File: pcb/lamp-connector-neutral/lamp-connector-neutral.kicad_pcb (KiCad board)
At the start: 2 copper layers, 17.8 x 29 mm, 2 parts

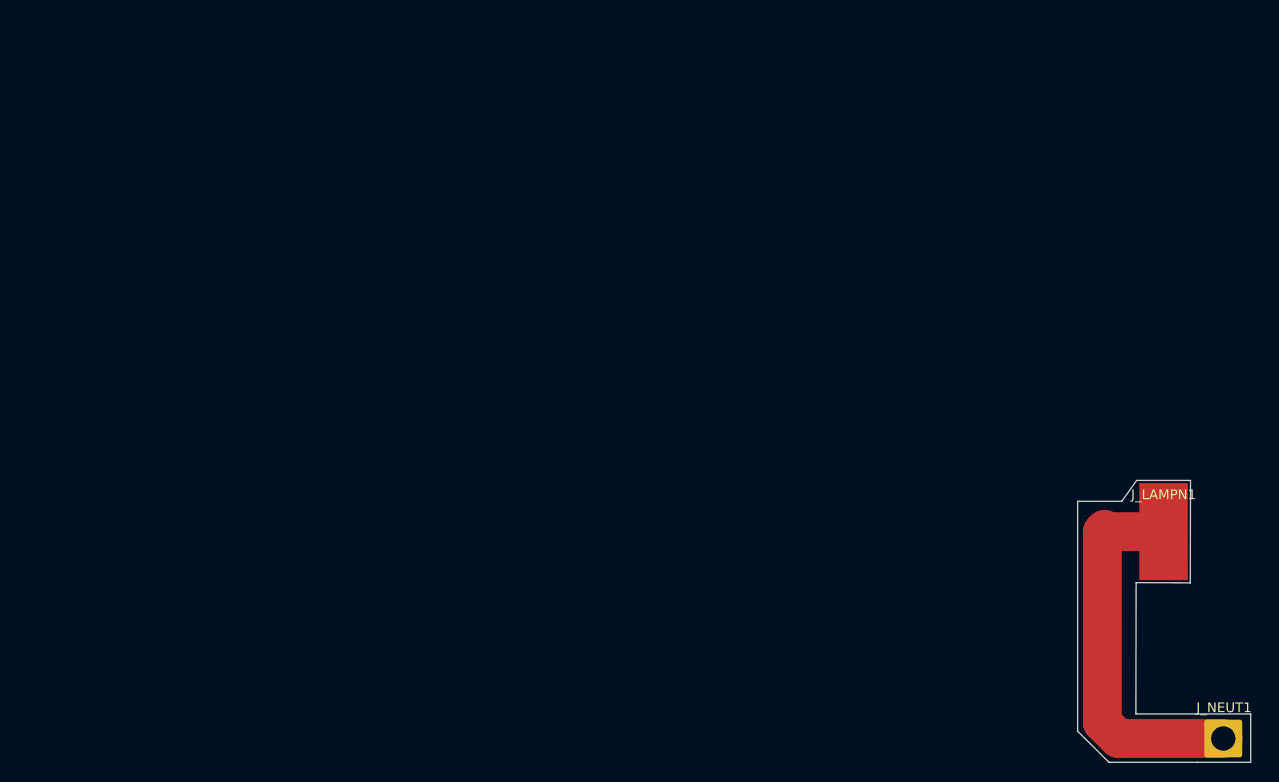
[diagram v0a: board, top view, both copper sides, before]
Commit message: Lamp Connectors
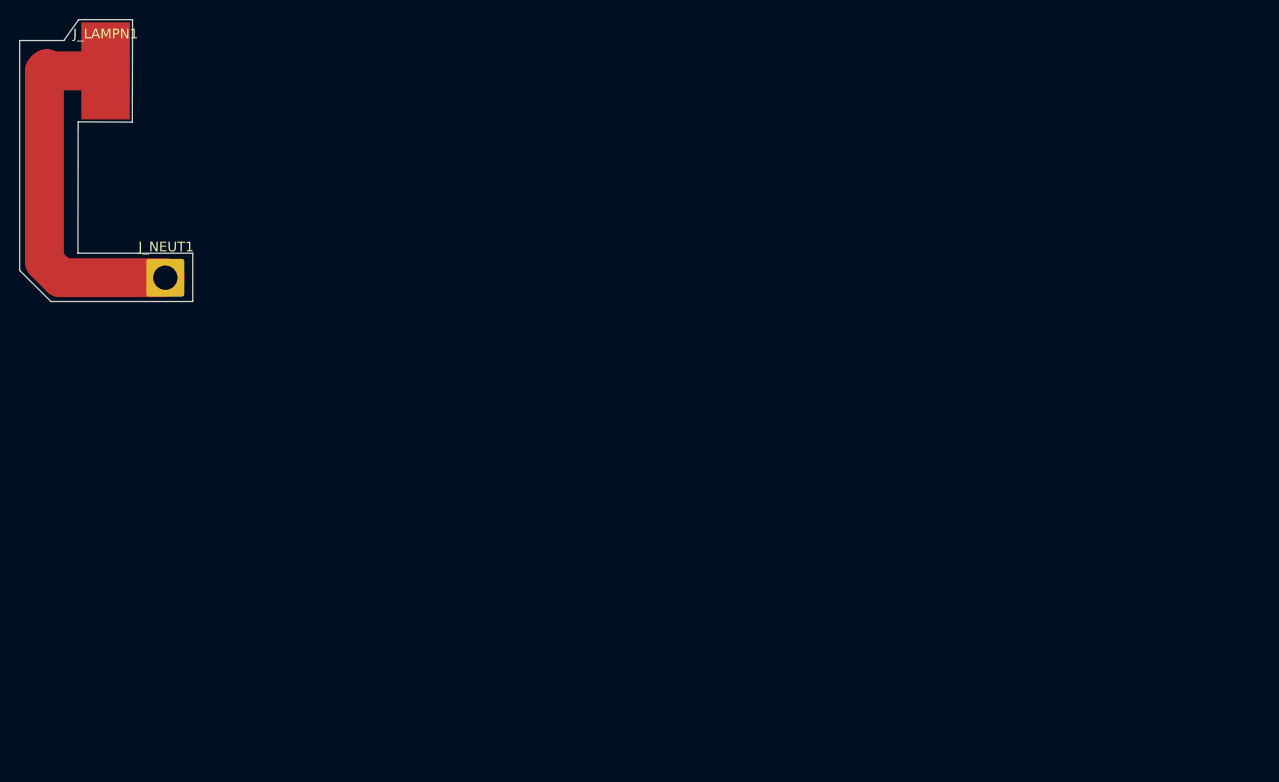
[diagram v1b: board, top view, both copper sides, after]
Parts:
- moved J_LAMPN1 118.8 mm to (8.85, 5.30)
- moved J_NEUT1 118.8 mm to (15.1, 26.6)
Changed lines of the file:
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@@
 		(pad_to_mask_clearance 0)
 		(allow_soldermask_bridges_in_footprints no)
+		(grid_origin 0 29.3)
 		(pcbplotparams
-			(layerselection 0x00010fc_ffffffff)
+			(layerselection 0x0000000_7fffffff)
 			(plot_on_all_layers_selection 0x0000000_00000000)
 			(disableapertmacros no)
@@
 			(viasonmask no)
 			(mode 1)
-			(useauxorigin no)
+			(useauxorigin yes)
 			(hpglpennumber 1)
 			(hpglpenspeed 20)
@@
 			(outputformat 1)
 			(mirror no)
-			(drillshape 1)
+			(drillshape 0)
 			(scaleselection 1)
 			(outputdirectory "")
@@
 	(footprint "Connector_Wire:SolderWirePad_1x01_SMD_5x10mm"
 		(layer "F.Cu")
-		(at 117.8 52.75)
+		(at 8.85 5.3)
 		(descr "Wire Pad, Square, SMD Pad,  5mm x 10mm,")
 		(tags "MesurementPoint Square SMDPad 5mmx10mm ")
@@
 	(footprint "Connector_Wire:SolderWire-2sqmm_1x01_D2mm_OD3.9mm"
 		(layer "F.Cu")
-		(at 124.025 74.025)
+		(at 15.075 26.575)
 		(descr "Soldered wire connection, for a single 2 mm² wire, reinforced insulation, conductor diameter 2mm, outer diameter 3.9mm, size source Multi-Contact FLEXI-xV 2.0 (https://ec.staubli.com/AcroFiles/Catalogues/TM_Cab-Main-11014119_(en)_hi.pdf), bend radius 3 times outer diameter, generated with kicad-footprint-generator")
 		(tags "connector wire 2sqmm")
@@
 	(gr_poly
 		(pts
-			(xy 124.006003 73.159799) (xy 124.061804 73.164998) (xy 124.117102 73.173799) (xy 124.171805 73.185998)
-			(xy 124.2256 73.2017) (xy 124.278403 73.220598) (xy 124.329802 73.242898) (xy 124.379706 73.2683)
-			(xy 124.428 73.296899) (xy 124.474303 73.328298) (xy 124.518607 73.362699) (xy 124.560606 73.399801)
-			(xy 124.600203 73.439397) (xy 124.637305 73.481401) (xy 124.671606 73.525701) (xy 124.703101 73.572)
-			(xy 124.731703 73.620298) (xy 124.757101 73.670198) (xy 124.779303 73.721601) (xy 124.7983 73.774297)
-			(xy 124.814001 73.828199) (xy 124.826201 73.882799) (xy 124.835005 73.938199) (xy 124.840201 73.994001)
-			(xy 124.842001 74.050001) (xy 124.840201 74.106) (xy 124.835005 74.161798) (xy 124.826201 74.2171)
-			(xy 124.814001 74.271799) (xy 124.7983 74.325597) (xy 124.779303 74.3784) (xy 124.757101 74.4298)
-			(xy 124.731703 74.4797) (xy 124.703101 74.527898) (xy 124.671606 74.5743) (xy 124.637305 74.6186)
-			(xy 124.600203 74.6606) (xy 124.560606 74.700201) (xy 124.518607 74.737298) (xy 124.474303 74.7716)
-			(xy 124.428 74.803098) (xy 124.379706 74.831701) (xy 124.329802 74.857099) (xy 124.278403 74.8794)
-			(xy 124.2256 74.898298) (xy 124.171805 74.913999) (xy 124.117102 74.926198) (xy 124.061804 74.934999)
-			(xy 124.006003 74.940198) (xy 123.950003 74.941999) (xy 123.894003 74.940198) (xy 123.838202 74.934999)
-			(xy 123.782904 74.926198) (xy 123.728201 74.913999) (xy 123.6743 74.898298) (xy 123.621603 74.8794)
-			(xy 123.570204 74.857099) (xy 123.5203 74.831701) (xy 123.472006 74.803098) (xy 123.425703 74.7716)
-			(xy 123.3814 74.737298) (xy 123.3394 74.700201) (xy 123.299704 74.6606) (xy 123.262701 74.6186) (xy 123.2284 74.5743)
-			(xy 123.196906 74.527898) (xy 123.168303 74.4797) (xy 123.142905 74.4298) (xy 123.120604 74.3784)
-			(xy 123.101706 74.325597) (xy 123.086005 74.271799) (xy 123.073805 74.2171) (xy 123.065001 74.161798)
-			(xy 123.059805 74.106) (xy 123.058005 74.050001) (xy 123.059805 73.994001) (xy 123.065001 73.938199)
-			(xy 123.073805 73.882799) (xy 123.086005 73.828199) (xy 123.101706 73.774297) (xy 123.120604 73.721601)
-			(xy 123.142905 73.670198) (xy 123.168303 73.620298) (xy 123.196906 73.572) (xy 123.2284 73.525701)
-			(xy 123.262701 73.481401) (xy 123.299704 73.439397) (xy 123.3394 73.399801) (xy 123.3814 73.362699)
-			(xy 123.425703 73.328298) (xy 123.472006 73.296899) (xy 123.5203 73.2683) (xy 123.570204 73.242898)
-			(xy 123.621603 73.220598) (xy 123.6743 73.2017) (xy 123.728201 73.185998) (xy 123.782904 73.173799)
-			(xy 123.838202 73.164998) (xy 123.894003 73.159799) (xy 123.950003 73.157999)
+			(xy 15.056003 25.709799) (xy 15.111804 25.714998) (xy 15.167102 25.723799) (xy 15.221805 25.735998)
+			(xy 15.2756 25.7517) (xy 15.328403 25.770598) (xy 15.379802 25.792898) (xy 15.429706 25.8183) (xy 15.478 25.846899)
+			(xy 15.524303 25.878298) (xy 15.568607 25.912699) (xy 15.610606 25.949801) (xy 15.650203 25.989397)
+			(xy 15.687305 26.031401) (xy 15.721606 26.075701) (xy 15.753101 26.122) (xy 15.781703 26.170298)
+			(xy 15.807101 26.220198) (xy 15.829303 26.271601) (xy 15.8483 26.324297) (xy 15.864001 26.378199)
+			(xy 15.876201 26.432799) (xy 15.885005 26.488199) (xy 15.890201 26.544001) (xy 15.892001 26.600001)
+			(xy 15.890201 26.656) (xy 15.885005 26.711798) (xy 15.876201 26.7671) (xy 15.864001 26.821799) (xy 15.8483 26.875597)
+			(xy 15.829303 26.9284) (xy 15.807101 26.9798) (xy 15.781703 27.0297) (xy 15.753101 27.077898) (xy 15.721606 27.1243)
+			(xy 15.687305 27.1686) (xy 15.650203 27.2106) (xy 15.610606 27.250201) (xy 15.568607 27.287298) (xy 15.524303 27.3216)
+			(xy 15.478 27.353098) (xy 15.429706 27.381701) (xy 15.379802 27.407099) (xy 15.328403 27.4294) (xy 15.2756 27.448298)
+			(xy 15.221805 27.463999) (xy 15.167102 27.476198) (xy 15.111804 27.484999) (xy 15.056003 27.490198)
+			(xy 15.000003 27.491999) (xy 14.944003 27.490198) (xy 14.888202 27.484999) (xy 14.832904 27.476198)
+			(xy 14.778201 27.463999) (xy 14.7243 27.448298) (xy 14.671603 27.4294) (xy 14.620204 27.407099) (xy 14.5703 27.381701)
+			(xy 14.522006 27.353098) (xy 14.475703 27.3216) (xy 14.4314 27.287298) (xy 14.3894 27.250201) (xy 14.349704 27.2106)
+			(xy 14.312701 27.1686) (xy 14.2784 27.1243) (xy 14.246906 27.077898) (xy 14.218303 27.0297) (xy 14.192905 26.9798)
+			(xy 14.170604 26.9284) (xy 14.151706 26.875597) (xy 14.136005 26.821799) (xy 14.123805 26.7671) (xy 14.115001 26.711798)
+			(xy 14.109805 26.656) (xy 14.108005 26.600001) (xy 14.109805 26.544001) (xy 14.115001 26.488199)
+			(xy 14.123805 26.432799) (xy 14.136005 26.378199) (xy 14.151706 26.324297) (xy 14.170604 26.271601)
+			(xy 14.192905 26.220198) (xy 14.218303 26.170298) (xy 14.246906 26.122) (xy 14.2784 26.075701) (xy 14.312701 26.031401)
+			(xy 14.349704 25.989397) (xy 14.3894 25.949801) (xy 14.4314 25.912699) (xy 14.475703 25.878298) (xy 14.522006 25.846899)
+			(xy 14.5703 25.8183) (xy 14.620204 25.792898) (xy 14.671603 25.770598) (xy 14.7243 25.7517) (xy 14.778201 25.735998)
+			(xy 14.832904 25.723799) (xy 14.888202 25.714998) (xy 14.944003 25.709799) (xy 15.000003 25.707999)
 		)
 		(stroke
@@
 	(gr_poly
 		(pts
-			(xy 119.9 56.2) (xy 119.100005 56.2) (xy 119.100005 49.900001) (xy 119.9 49.900001)
+			(xy 10.95 8.75) (xy 10.150005 8.75) (xy 10.150005 2.450001) (xy 10.95 2.450001)
 		)
 		(stroke
@@
 	(gr_poly
 		(pts
-			(xy 120.575 47.475) (xy 120.55 58.025) (xy 114.975 58) (xy 114.95 71.525) (xy 121.3 71.525) (xy 126.775 71.525)
-			(xy 126.775 76.5) (xy 121.275 76.5) (xy 112.175 76.5) (xy 108.95 73.3) (xy 108.95 49.625) (xy 113.5 49.625)
-			(xy 115.025 47.475)
+			(xy 11.625 0.025) (xy 11.6 10.575) (xy 6.025 10.55) (xy 6 24.075) (xy 12.35 24.075) (xy 17.825 24.075)
+			(xy 17.825 29.05) (xy 12.325 29.05) (xy 3.225 29.05) (xy 0 25.85) (xy 0 2.175) (xy 4.55 2.175) (xy 6.075 0.025)
 		)
 		(stroke
@@
 	)
 	(gr_rect
-		(start 118.75 49.55)
-		(end 120.25 56.55)
+		(start 9.8 2.1)
+		(end 11.3 9.1)
 		(stroke
 			(width 0.1)
@@
 		(layer "Dwgs.User")
 		(pts
-			(xy 123.950003 74.941999) (xy 123.950003 73.157999)
+			(xy 15.000003 27.491999) (xy 15.000003 25.707999)
 		)
 		(height -4.500003)
 		(gr_text "1.7840 mm"
-			(at 118.3 74.049999 90)
+			(at 9.35 26.599999 90)
 			(layer "Dwgs.User")
 			(effects
@@
 		(layer "Dwgs.User")
 		(pts
-			(xy 123.058005 74.050001) (xy 124.842001 74.050001)
+			(xy 14.108005 26.600001) (xy 15.892001 26.600001)
 		)
 		(height -3.750001)
 		(gr_text "1.7840 mm"
-			(at 123.950003 69.15 0)
+			(at 15.000003 21.7 0)
 			(layer "Dwgs.User")
 			(effects
@@
 	)
 	(segment
-		(start 111.5 72.4)
-		(end 111.5 52.775)
+		(start 2.55 24.95)
+		(end 2.55 5.325)
 		(width 4)
 		(layer "F.Cu")
@@
 	)
 	(segment
-		(start 111.75 52.525)
-		(end 111.975 52.75)
+		(start 2.8 5.075)
+		(end 3.025 5.3)
 		(width 4)
 		(layer "F.Cu")
@@
 	)
 	(segment
-		(start 111.5 52.775)
-		(end 111.75 52.525)
+		(start 2.55 5.325)
+		(end 2.8 5.075)
 		(width 4)
 		(layer "F.Cu")
@@
 	)
 	(segment
-		(start 113.15 74.05)
-		(end 111.5 72.4)
+		(start 4.2 26.6)
+		(end 2.55 24.95)
 		(width 4)
 		(layer "F.Cu")
@@
 	)
 	(segment
-		(start 123.95 74.05)
-		(end 113.15 74.05)
+		(start 15 26.6)
+		(end 4.2 26.6)
 		(width 4)
 		(layer "F.Cu")
@@
 	)
 	(segment
-		(start 111.975 52.75)
-		(end 117.8 52.75)
-		(width 4)
-		(layer "F.Cu")
+		(start 3.025 5.3)
+		(end 8.85 5.3)
+		(width 4)
+		(layer "F.Cu")
